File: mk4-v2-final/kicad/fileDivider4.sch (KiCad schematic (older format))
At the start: 3 parts

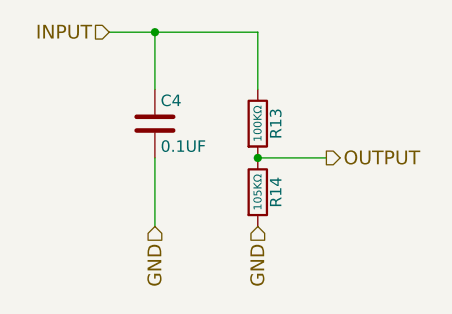
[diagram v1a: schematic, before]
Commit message: added headnight diodes, I don't think software control of them is going to be possible
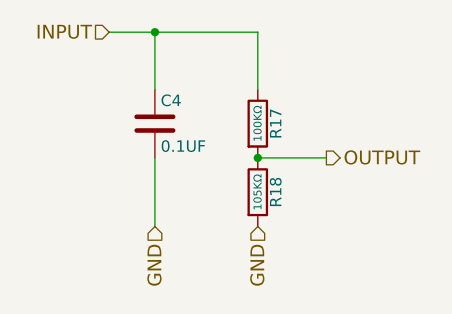
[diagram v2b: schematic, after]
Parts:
- renumbered R13 to R17, R14 to R18
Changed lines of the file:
@@
 $EndDescr
 $Comp
-L R R14
+L R R18
 U 1 1 59DEA271
 P 5650 3850
-F 0 "R14" V 5730 3850 50  0000 C CNN
+F 0 "R18" V 5730 3850 50  0000 C CNN
 F 1 "105KΩ" V 5650 3850 35  0000 C CNN
 F 2 "Resistors_THT:R_Axial_DIN0207_L6.3mm_D2.5mm_P10.16mm_Horizontal" V 5580 3850 50  0001 C CNN
@@
 OUTPUT
 $Comp
-L R R13
+L R R17
 U 1 1 59DEA293
 P 5650 3550
-F 0 "R13" V 5730 3550 50  0000 C CNN
+F 0 "R17" V 5730 3550 50  0000 C CNN
 F 1 "100KΩ" V 5650 3550 35  0000 C CNN
 F 2 "Resistors_THT:R_Axial_DIN0207_L6.3mm_D2.5mm_P10.16mm_Horizontal" V 5580 3550 50  0001 C CNN

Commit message: schematic is done, footprint association and netlist are also done
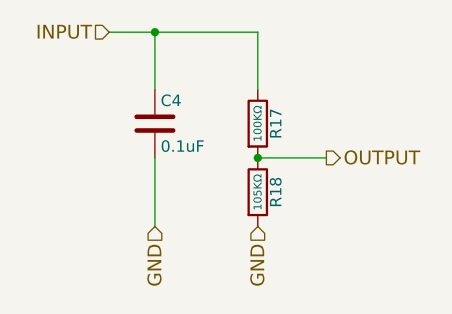
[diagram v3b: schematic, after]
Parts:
- C4: value 0.1UF -> 0.1uF; footprint Capacitors_THT:CP_Radial_D5.0mm_P2.00mm -> C_Rect_L5.08mm_W3.175mm_P2.54mm:C_Rect_L5.08mm_W3.175mm_P2.54mm; digikey-pn (none) -> 478-5096-ND; mfg-pn (none) -> AR205F104K4R
- R17: footprint Resistors_THT:R_Axial_DIN0207_L6.3mm_D2.5mm_P10.16mm_Horizontal -> Resistors_THT:R_Axial_DIN0204_L3.6mm_D1.6mm_P5.08mm_Horizontal; digikey-pn (none) -> BC100KXCT-ND; mfg-pn (none) -> MBA02040C1003FRP00
- R18: footprint Resistors_THT:R_Axial_DIN0207_L6.3mm_D2.5mm_P10.16mm_Horizontal -> Resistors_THT:R_Axial_DIN0204_L3.6mm_D1.6mm_P5.08mm_Horizontal; digikey-pn (none) -> 105KXBK-ND; mfg-pn (none) -> MFR-25FBF52-105K
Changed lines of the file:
@@
 EESchema Schematic File Version 2
-LIBS:hitchco-mk4-rescue
 LIBS:power
 LIBS:device
@@
 LIBS:cd4013b
 LIBS:ncs3s1205sc
+LIBS:lca715
+LIBS:SN74HC595N
+LIBS:CD74HC4067
 LIBS:hitchco-mk4-cache
 EELAYER 25 0
@@
 F 0 "R18" V 5730 3850 50  0000 C CNN
 F 1 "105KΩ" V 5650 3850 35  0000 C CNN
-F 2 "Resistors_THT:R_Axial_DIN0207_L6.3mm_D2.5mm_P10.16mm_Horizontal" V 5580 3850 50  0001 C CNN
+F 2 "Resistors_THT:R_Axial_DIN0204_L3.6mm_D1.6mm_P5.08mm_Horizontal" V 5580 3850 50  0001 C CNN
 F 3 "" H 5650 3850 50  0001 C CNN
+F 4 "105KXBK-ND" H 5730 3950 50  0001 C CNN "digikey-pn"
+F 5 "MFR-25FBF52-105K" H 5730 3950 50  0001 C CNN "mfg-pn"
 	1    5650 3850
 	1    0    0    -1
 $EndComp
-Text HLabel 5950 3700 2    60   Output ~ 0
-OUTPUT
 $Comp
 L R R17
@@
 F 0 "R17" V 5730 3550 50  0000 C CNN
 F 1 "100KΩ" V 5650 3550 35  0000 C CNN
-F 2 "Resistors_THT:R_Axial_DIN0207_L6.3mm_D2.5mm_P10.16mm_Horizontal" V 5580 3550 50  0001 C CNN
+F 2 "Resistors_THT:R_Axial_DIN0204_L3.6mm_D1.6mm_P5.08mm_Horizontal" V 5580 3550 50  0001 C CNN
 F 3 "" H 5650 3550 50  0001 C CNN
+F 4 "BC100KXCT-ND" H 5730 3650 50  0001 C CNN "digikey-pn"
+F 5 "MBA02040C1003FRP00" H 5730 3650 50  0001 C CNN "mfg-pn"
 	1    5650 3550
 	1    0    0    -1
 $EndComp
+$Comp
+L C C4
+U 1 1 5A24190E
+P 5200 3550
+F 0 "C4" H 5225 3650 50  0000 L CNN
+F 1 "0.1uF" H 5225 3450 50  0000 L CNN
+F 2 "C_Rect_L5.08mm_W3.175mm_P2.54mm:C_Rect_L5.08mm_W3.175mm_P2.54mm" H 5238 3400 50  0001 C CNN
+F 3 "http://datasheets.avx.com/AR-Series.pdf" H 5200 3550 50  0001 C CNN
+F 4 "478-5096-ND" H 5225 3750 50  0001 C CNN "digikey-pn"
+F 5 "AR205F104K4R" H 5225 3750 50  0001 C CNN "mfg-pn"
+	1    5200 3550
+	1    0    0    -1
+$EndComp
+Text HLabel 5950 3700 2    60   Output ~ 0
+OUTPUT
+Text HLabel 5000 3150 0    60   Input ~ 0
+INPUT
+Text HLabel 5650 4000 3    60   Input ~ 0
+GND
+Text HLabel 5200 4000 3    60   Input ~ 0
+GND
 Wire Wire Line
 	5200 3700 5200 4000
@@
 Wire Wire Line
 	5200 3150 5200 3400
-Connection ~ 5200 3150
 Wire Wire Line
 	5950 3700 5650 3700
+Connection ~ 5200 3150
 Connection ~ 5650 3700
-Text HLabel 5000 3150 0    60   Input ~ 0
-INPUT
-Text HLabel 5650 4000 3    60   Input ~ 0
-GND
-Text HLabel 5200 4000 3    60   Input ~ 0
-GND
-$Comp
-L C C4
-U 1 1 5A24190E
-P 5200 3550
-F 0 "C4" H 5225 3650 50  0000 L CNN
-F 1 "0.1UF" H 5225 3450 50  0000 L CNN
-F 2 "Capacitors_THT:CP_Radial_D5.0mm_P2.00mm" H 5238 3400 50  0001 C CNN
-F 3 "http://nichicon-us.com/english/products/pdfs/e-uvr.pdf" H 5200 3550 50  0001 C CNN
-	1    5200 3550
-	1    0    0    -1
-$EndComp
 $EndSCHEMATC
